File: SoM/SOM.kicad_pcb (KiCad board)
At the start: 6 copper layers, 67.6 x 50 mm, 135 parts, among them J1 SODIMM-200_Split, Q1 BC847, Q2 BC847, U1 CCGM1A1, U2 MX25V8035F, U3 74LVC2G53, U4 MPM3833C, U5 MPM3833C, X1 ECS-5032MV

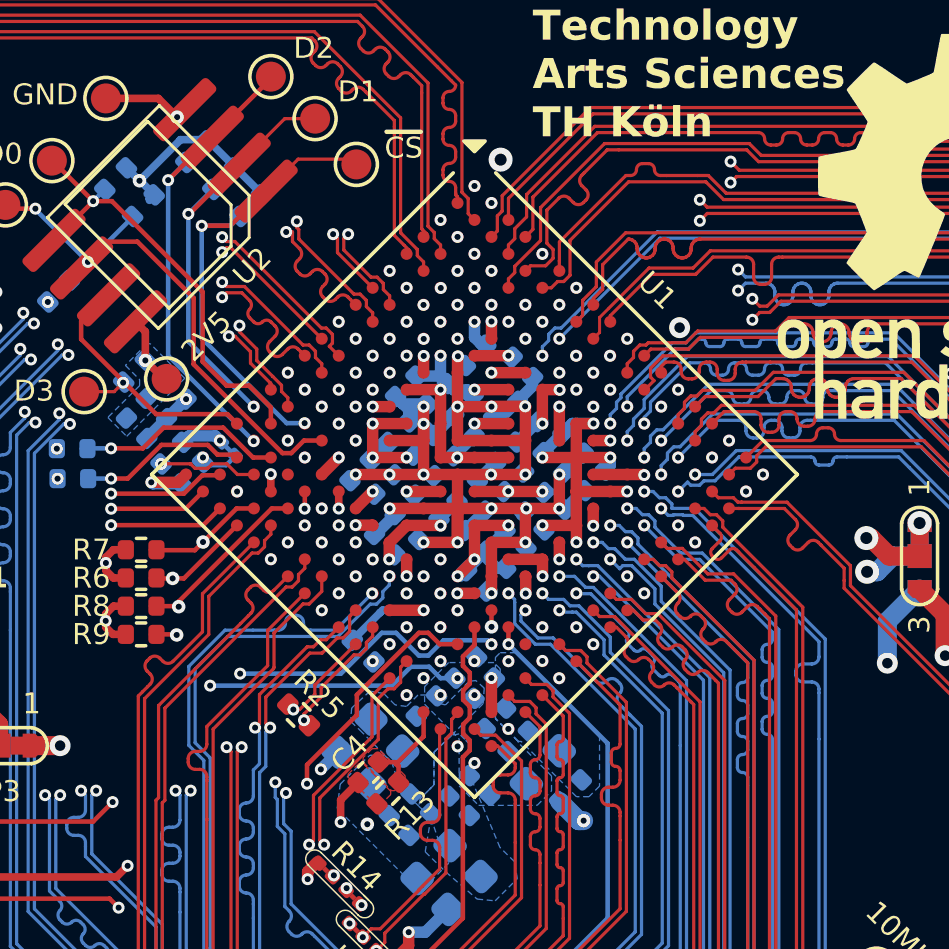
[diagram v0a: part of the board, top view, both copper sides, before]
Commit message: Use custom BGA-324 footprint with embedded 3D model
- Replace generic Package_BGA KiCad footprint with own
  ccsom_Footprint_lib:BGA-324_15x15mm_Layout18x18_P0.8mm,
  matching the actual GateMate BGA-324 pinout
- Add Ironwood-BGA-324-Socket footprint to the library
- Embed CCGM1A1_2.step directly in the footprint instead of
  referencing a separate 3D model file
- Make fp-lib-table and sym-lib-table paths portable via
  ${KIPRJMOD} instead of a hardcoded local path
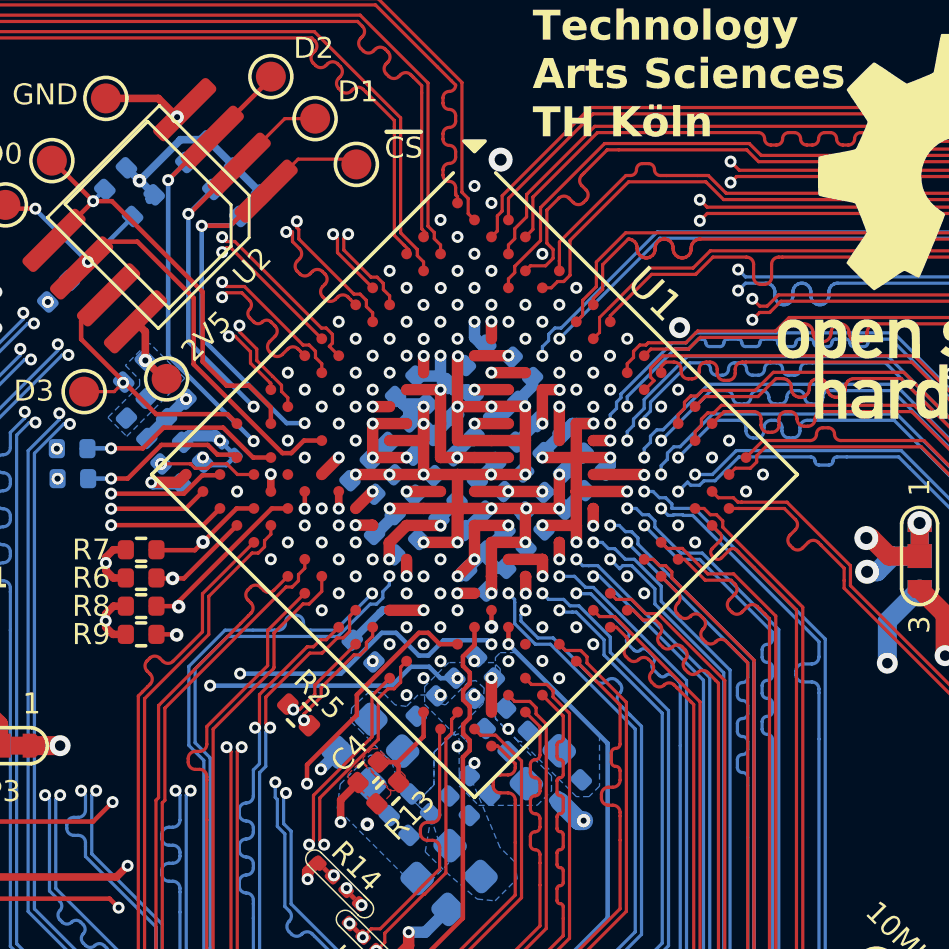
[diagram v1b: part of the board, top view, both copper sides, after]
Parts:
- U1: footprint Package_BGA:BGA-324_15.0x15.0mm_Layout18x18_P0.8mm_Ball0.45mm_Pad0.4mm_NSMD -> ccsom_Footprint_lib:BGA-324_15x15mm_Layout18x18_P0.8mm
